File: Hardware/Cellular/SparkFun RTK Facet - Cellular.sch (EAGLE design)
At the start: 64 parts, among them IC1 SN74AVC4T774PW, J1 FPC_12_0.5MM_BACKFLIP, J18 SARA_USB, J2 NANO_SIM, J3 U.FL, J6 DIAG, Q2 310mA/60V/1.6Ω, Q3 310mA/60V/1.6Ω, Q4 310mA/60V/1.6Ω, Q5 20V/0.2A/8MHz/1.2Ω/1Vth, Q7 310mA/60V/1.6Ω, U1 SARA-R510M8S, U8 74HC1G04

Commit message: Paul edits. Move dummy to sub-folder
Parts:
- removed C19: 27pF, New_Parts:27PF-0402-25V-5%-X7R
- removed C22: 0.1uF, SparkFun-Capacitors:0.1UF-0603-25V-(+80/-20%)
- removed C24: 15pF, SparkFun-Capacitors:15PF-0603-50V-5%
- removed D10: PESD0402, New_Parts:PESD0402
- removed D13: BLUE, SparkFun-LED:LED-BLUE0603
- removed D14: WHITE, SparkFun-LED:LED-WHITE0603
- removed D8: DT1042-04SO-7, ublox:TVS_DIODE_ARRAY_4DT1042-04SO-7
- removed FRAME1: FRAME-LETTER, SparkFun-Aesthetics:FRAME-LETTER
- removed FRAME2: FRAME-LETTERNO_PACKAGE, SparkFun-Aesthetics:FRAME-LETTERNO_PACKAGE
- removed J18: SARA_USB, SparkFun-Connectors:CONN_041X04_NO_SILK
- removed J6: DIAG, SparkFun-Connectors:CONN_05NO_SILK
- removed JP19: JUMPER-SMT_3_1-NC_TRACE_SILK, SparkFun-Jumpers:JUMPER-SMT_3_1-NC_TRACE_SILK
- removed L2: 68nH, New_Parts:68NH-0402
- removed Q4, Q7: 310mA/60V/1.6Ω, SparkFun-DiscreteSemi:MOSFET-NCH-2N7002PW
- removed Q5: 20V/0.2A/8MHz/1.2Ω/1Vth, SparkFun-DiscreteSemi:MOSFET-NCH-RE1C00UNTL
- removed R18, R19, R39, R44: 100k, SparkFun-Resistors:100KOHM-0603-1/10W-1%
- removed R23: 10k, SparkFun-Resistors:10KOHM-0603-1/10W-1%
- removed R27, R28, R34, R42, R43: 1k, SparkFun-Resistors:1KOHM-0603-1/10W-1%
- removed R29, R30: 2.2k, SparkFun-Resistors:2.2KOHM-0603-1/10W-1%
- removed R31: 0, SparkFun-Resistors:0OHM-0603-1/10W
- removed R35: 470, SparkFun-Resistors:470OHM-0603-1/10W-1%
- removed TP13: TEST-POINT3, SparkFun-Connectors:TEST-POINT3
- removed U8: 74HC1G04, SparkFun-IC-Logic:74HC1G04
- added C1, C17, C3: 1.0uF, SparkFun-Capacitors:1.0UF-0603-16V-10%-X7R
- added C13: 33pF, New_Parts:33PF-0402-25V-5%-X7R
- added C2, C4, C5, C6: 0.1uF, SparkFun-Capacitors:0.1UF-0603-25V-5%
- added C9: 47pF, SparkFun-Capacitors:47PF-0603-50V-5%
- added D1: PESD0402, New_Parts:PESD0402
- added D2: DT1042-04SO-7, ublox:TVS_DIODE_ARRAY_4DT1042-04SO-7
- added FRAME3: FRAME-LEDGER, SparkFun-Aesthetics:FRAME-LEDGER
- added J4: (no value), SparkFun-Connectors:SIMHOLDER-PUSHPUSH
- added LOGO1: SPECIAL_INSTRUCTIONS-ORDERING, SparkFun-Aesthetics:SPECIAL_INSTRUCTIONS-ORDERING
- added Q1: 20V/0.2A/8MHz/1.2Ω/1Vth, SparkFun-DiscreteSemi:MOSFET-NCH-RE1C002UNTCL
- added R1, R2, R3: 100k, SparkFun-Resistors:100KOHM-0603-1/10W-1%
- added R4, R5: 1k, SparkFun-Resistors:1KOHM-0603-1/10W-1%
- added R6, R7: 2.2k, SparkFun-Resistors:2.2KOHM-0603-1/10W-1%
- added R8: 0, SparkFun-Resistors:0OHM-0603-1/10W
- added TP10, TP11, TP9: TEST-POINT3, SparkFun-Connectors:TEST-POINT3
- added U2: 74HC1G04, SparkFun-IC-Logic:74HC1G04
- added U3: AP2112K-3.3, SparkFun-IC-Power:V_REG_AP2112K-3.3V
- C11: value 47pF -> 68pF; device SparkFun-Capacitors:47PF-0603-50V-5% -> SparkFun-Capacitors:68PF-0603-50V-5%
- C12: value 0.1uF -> 10uF; device SparkFun-Capacitors:0.1UF-0603-25V-5% -> SparkFun-Capacitors:10UF-0603-6.3V-20%
- C14: device SparkFun-Capacitors:0.1UF-0603-25V-5% -> SparkFun-Capacitors:0.1UF-0603-25V-(+80/-20%)
- C15: value 68pF -> 15pF; device SparkFun-Capacitors:68PF-0603-50V-5% -> SparkFun-Capacitors:15PF-0603-50V-5%
- C16: value 10uF -> 0.1uF; device SparkFun-Capacitors:10UF-0603-6.3V-20% -> SparkFun-Capacitors:0.1UF-0603-25V-(+80/-20%)
- C18: value 33pF -> 0.1uF; device New_Parts:33PF-0402-25V-5%-X7R -> SparkFun-Capacitors:0.1UF-0603-25V-5%
- J2: value NANO_SIM -> U.FL; device ublox:NANO_SIMWURTH -> SparkFun-Connectors:U.FL2PIN
- J3: value U.FL -> DIAG; device SparkFun-Connectors:U.FL2PIN -> SparkFun-Connectors:CONN_06NO_SILK_FEMALE_PTH
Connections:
- removed net 1.8V: J6.4
- removed net LTE_NI: Q3.D, R35.1, R39.1
- removed net N$16: C19.1, D10.1, L2.1, R23.2
- removed net N$35: Q3.G, R34.2
- removed net N$37: D13.C, R35.2
- removed net N$43: JP19.2, Q5.S, R29.1
- removed net N$47: Q7.G, R42.2
- removed net N$49: D14.C, R43.2
- removed net SARA_!ON!: Q7.D, R43.1, R44.1, TP13.1
- removed net SARA_ANT_DET: R23.1, U1.ANT_DET
- removed net SARA_GPIO3: JP19.1
- removed net SARA_NI: R34.1, U1.GPIO1
- removed net SARA_TP: U1.GPIO6/TP
- removed net SARA_USB_D+: J18.2, U1.USB_D+
- removed net SARA_USB_D-: J18.1, U1.USB_D-
- removed net SARA_VUSB_DET: J18.3, U1.VUSB_DET
- removed net VIN: J6.1
- new net MAIN_3V3: J1.10, J1.9, R1.2, U3.EN
- new net N$1: TP9.1, U1.USB_D-
- new net N$2: TP10.1, U1.USB_D+
- new net N$3: TP11.1, U1.VUSB_DET
- net 3.3V: now also C11.1, C12.1, C3.1, C4.2, C6.1, J3.2, R7.2, U2G2.P$V+, U3.OUT; no longer C14.1, C24.1, D13.A, D14.A, J1.3, J1.4, J6.2, R30.2, R39.2, R44.2, U8G2.P$V+
- net GND: now also C1.2, C11.2, C12.2, C17.2, C18.1, C2.1, C3.2, C4.1, C5.1, C6.2, C9.1, D1.2, D2.2, D2.5, J1.11, J1.12, J3.6, J4.GND, R1.1, R2.2, R3.1, U1.DTR_I, U2G2.P$V-, U3.GND; no longer C11.1, C12.1, C19.2, C22.2, C24.2, D10.2, D8.2, D8.5, J1.1, J1.2, J18.4, J3.GND, J6.5, Q4.S, Q7.S, R18.2, R19.1, U8G2.P$V-
- net LTE_!RESET!: now also J1.8, U2G1.A; no longer J1.5, U8G1.A
- net LTE_CTSI: now also J1.5, R3.2; no longer J1.8, R19.2
- net LTE_INT: now also J1.6, Q1.D, R7.1; no longer J1.7, Q5.D, R30.1
- net LTE_PWR_ON: now also J1.7, R2.1, R4.1; no longer J1.6, R18.1, R27.1
- net LTE_RTSO: now also J1.4; no longer J1.9
- net LTE_RXI: now also J1.3, J3.4; no longer J1.10
- net LTE_TXO: now also J1.2, J3.5; no longer J1.11
- net N$15: now also C13.2, D1.1, J2.SIGNAL; no longer C18.2, J3.SIGNAL, L2.2
- net N$26: now also R4.2; no longer R27.2
- net N$27: now also Q3.G, R5.2; no longer Q4.G, R28.2
- net N$28: now also R5.1, U2G1.Y; no longer R28.1, U8G1.Y
- net N$31: now also C17.1, C18.2, R8.2; no longer R31.2
- net SARA_!RESET!: now also Q3.D; no longer Q4.D
- net SARA_ANT: now also C13.1; no longer C18.1
- net SARA_EXT_INT: now also Q1.S, R6.1; no longer JP19.3
- net SIM_CLK: now also D2.4, J4.CLK; no longer D8.1, J2.CLK
- net SIM_IO: now also D2.6, J4.I/O; no longer D8.6, J2.IO
- net SIM_RST: now also D2.3, J4.RST; no longer D8.4, J2.RST
- net VCCIO: now also C14.1, J3.3, Q1.G, R6.2, R8.1; no longer C22.1, J6.3, Q5.G, R29.2, R31.1, R42.1
- net VOUT: now also C1.1, C2.2, J1.1, J3.1, U3.IN; no longer J1.12
- net VSIM: now also C5.2, C9.2, D2.1, J4.VCC; no longer C11.2, C12.2, D8.3, J2.VCC
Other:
- note added: "600mA Max 55uA Quiescent"
- note added: "JLCPCB JLC7628 4-layer Impedance Control"
- note added: "Paul Clark"
- note added: "VCC: Min. 3.3V Typ. 3.8V Max. 4.4V VCC Extended: Min. 3.0V Max. 4.5V Worst case: Maximum current draw during Tx: 395mA AP2112-3.3 drop out voltage: ~175mV at: 400mA output current; Vout = 3.3V; 25°C Typical: Typical current draw during Tx/Rx: 195mA at 23dBm AP2112-3.3 drop out voltage: ~125mV at: 300mA output current; Vout = 3.3V; 25°C"
- note added: "Voltage Regulation"
- note removed: "SARA LEDs"
- note removed: "VCC: Min. 3.3V Typ. 3.8V Max. 4.4V VCC Extended: Min. 3.0V Max. 4.5V Worst case: Maximum current draw during Tx: 395mA Estimated current for other components: 100mA Total maximum current draw: ~500mA AP7361C-33 drop out voltage: ~170mV at: 500mA output current; Vout = 3.3V; 25°C D7 LSM115J Schottky diode forward voltage: ~210mV at: 500mA; 25°C AP7361C 3.3V output will start to fall when the batte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"

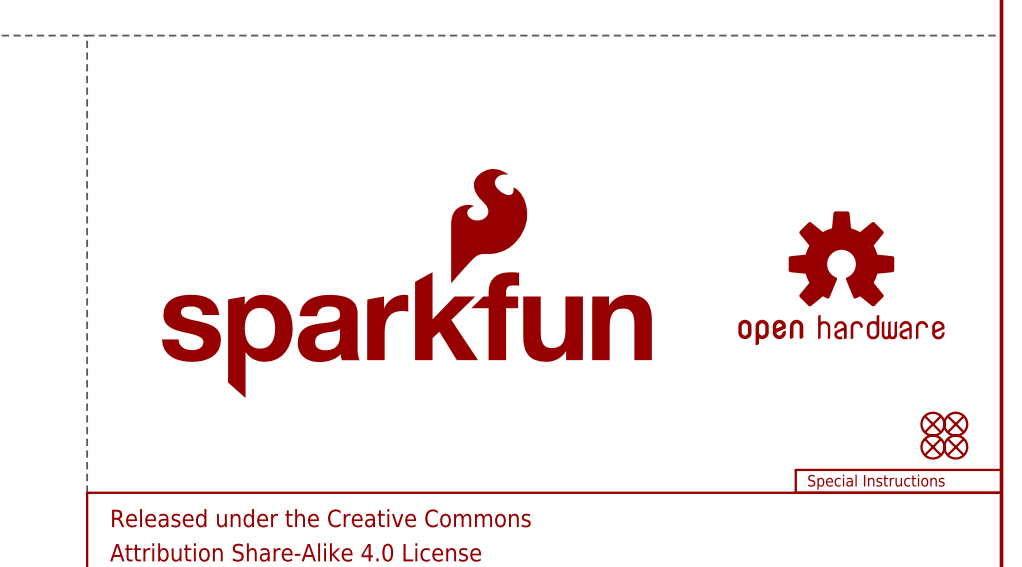
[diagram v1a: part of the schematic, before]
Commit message: Add Buzzard text
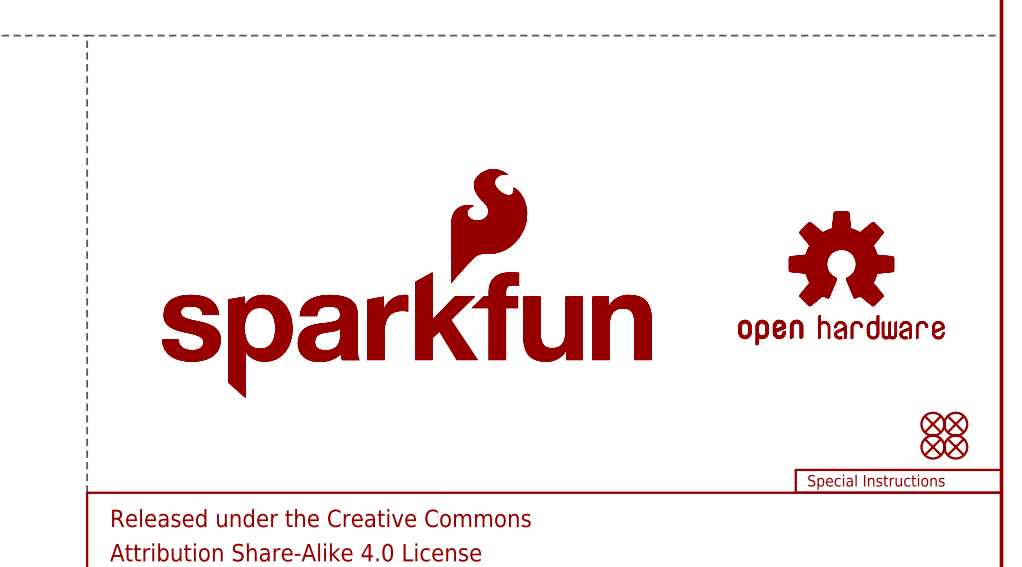
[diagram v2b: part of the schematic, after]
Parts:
- added LOGO2: SFE_LOGO_NAME_FLAME.1_INCH, SparkFun-Aesthetics:SFE_LOGO_NAME_FLAME.1_INCH
- added LOGO4: OSHW-LOGOMINI, SparkFun-Aesthetics:OSHW-LOGOMINI
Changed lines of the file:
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@@
 <part name="GND8" library="SparkFun-PowerSymbols" deviceset="GND" device=""/>
 <part name="GND9" library="SparkFun-PowerSymbols" deviceset="GND" device=""/>
+<part name="LOGO2" library="SparkFun-Aesthetics" deviceset="SFE_LOGO_NAME_FLAME" device=".1_INCH"/>
+<part name="LOGO4" library="SparkFun-Aesthetics" deviceset="OSHW-LOGO" device="MINI" value="OSHW-LOGOMINI"/>
 </parts>
 <sheets>
@@
 <attribute name="VALUE" x="55.88" y="220.726" size="1.778" layer="96" align="top-center"/>
 </instance>
+<instance part="LOGO2" gate="G$1" x="337.82" y="45.72" smashed="yes"/>
+<instance part="LOGO4" gate="G$1" x="414.02" y="60.96" smashed="yes"/>
 </instances>
 <busses>

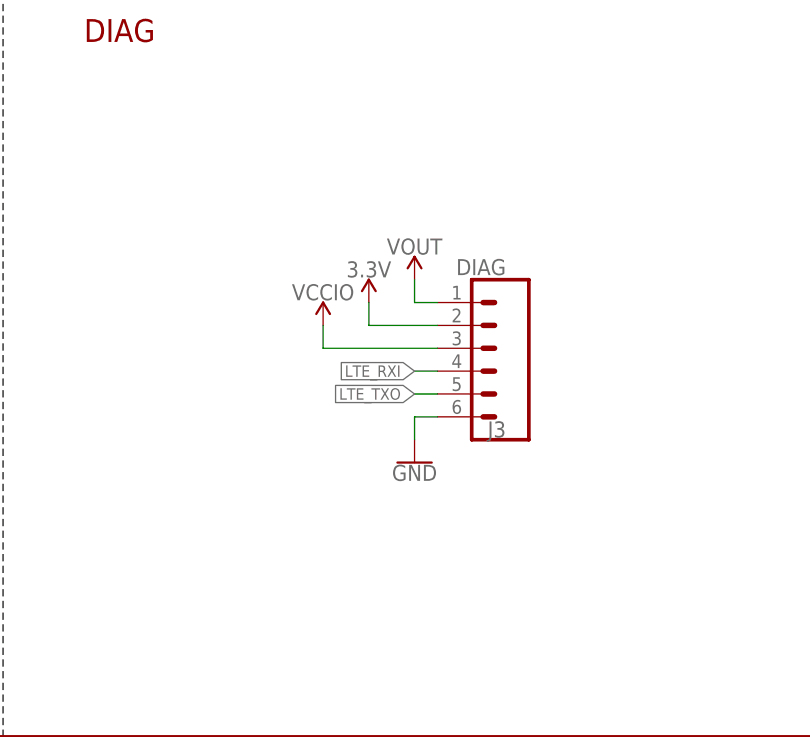
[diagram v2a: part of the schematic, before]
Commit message: Add cellular board production files
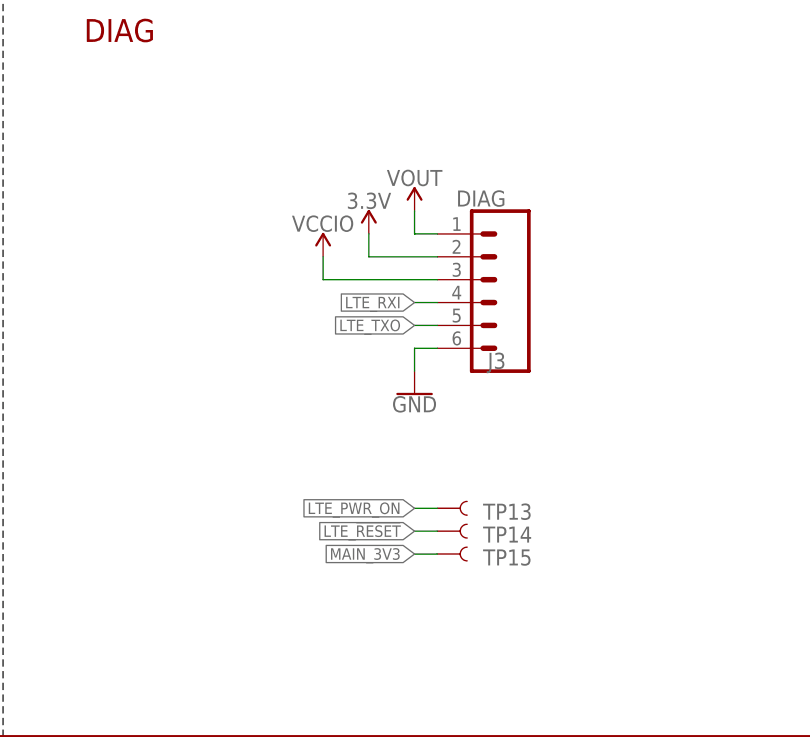
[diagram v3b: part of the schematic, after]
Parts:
- added TP13, TP14, TP15: TEST-POINT3, SparkFun-Connectors:TEST-POINT3
- J4: device SparkFun-Connectors:SIMHOLDER-PUSHPUSH -> SparkFun-Connectors:SIMHOLDER-PUSHPUSH-REDUCED-PADS
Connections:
- net LTE_!RESET!: now also TP14.1
- net LTE_PWR_ON: now also TP13.1
- net MAIN_3V3: now also TP15.1
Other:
- moved on the sheet: J3
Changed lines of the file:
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@@
 <setting verticaltext="up"/>
 </settings>
-<grid distance="0.1" unitdist="inch" unit="inch" style="lines" multiple="1" display="no" altdistance="0.05" altunitdist="inch" altunit="inch"/>
+<grid distance="0.05" unitdist="inch" unit="inch" style="lines" multiple="1" display="yes" altdistance="0.005" altunitdist="inch" altunit="inch"/>
 <layers>
 <layer number="1" name="Top" color="4" fill="1" visible="no" active="no"/>
@@
 <layer number="154" name="FabDoc2" color="7" fill="1" visible="yes" active="yes"/>
 <layer number="155" name="FabDoc3" color="7" fill="1" visible="yes" active="yes"/>
+<layer number="156" name="gesam-Maß" color="1" fill="7" visible="no" active="no"/>
+<layer number="157" name="FaceMchng" color="3" fill="1" visible="no" active="no"/>
+<layer number="158" name="FaceMMeas" color="3" fill="1" visible="no" active="no"/>
+<layer number="159" name="Geh-Bear2" color="1" fill="7" visible="no" active="no"/>
+<layer number="160" name="Topologie" color="9" fill="1" visible="no" active="no"/>
+<layer number="161" name="tomplace2" color="7" fill="1" visible="no" active="no"/>
 <layer number="166" name="AntennaArea" color="7" fill="1" visible="no" active="no"/>
 <layer number="168" name="4mmHeightArea" color="7" fill="1" visible="no" active="no"/>
@@
 <layer number="250" name="Descript" color="7" fill="1" visible="yes" active="yes"/>
 <layer number="251" name="SMDround" color="7" fill="1" visible="yes" active="yes"/>
+<layer number="252" name="BR-BS" color="7" fill="1" visible="no" active="no"/>
 <layer number="253" name="Extra" color="7" fill="1" visible="no" active="no"/>
 <layer number="254" name="cooling" color="7" fill="1" visible="yes" active="yes"/>
@@
 <part name="J2" library="SparkFun-Connectors" deviceset="U.FL2PIN" device="" value="U.FL"/>
 <part name="SUPPLY1" library="SparkFun-PowerSymbols" deviceset="VOUT" device=""/>
-<part name="J4" library="SparkFun-Connectors" deviceset="SIMHOLDER" device="-PUSHPUSH"/>
+<part name="J4" library="SparkFun-Connectors" deviceset="SIMHOLDER" device="-PUSHPUSH-REDUCED-PADS"/>
 <part name="FRAME3" library="SparkFun-Aesthetics" deviceset="FRAME-LEDGER" device=""/>
 <part name="LOGO1" library="SparkFun-Aesthetics" deviceset="SPECIAL_INSTRUCTIONS" device="-ORDERING"/>
@@
 <part name="LOGO2" library="SparkFun-Aesthetics" deviceset="SFE_LOGO_NAME_FLAME" device=".1_INCH"/>
 <part name="LOGO4" library="SparkFun-Aesthetics" deviceset="OSHW-LOGO" device="MINI" value="OSHW-LOGOMINI"/>
+<part name="TP13" library="SparkFun-Connectors" deviceset="TEST-POINT" device="3" value="TEST-POINT3"/>
+<part name="TP14" library="SparkFun-Connectors" deviceset="TEST-POINT" device="3" value="TEST-POINT3"/>
+<part name="TP15" library="SparkFun-Connectors" deviceset="TEST-POINT" device="3" value="TEST-POINT3"/>
 </parts>
 <sheets>
@@
 <attribute name="VALUE" x="332.74" y="134.366" size="1.778" layer="96" align="top-center"/>
 </instance>
-<instance part="J3" gate="G$1" x="287.02" y="43.18" smashed="yes" rot="R180">
-<attribute name="VALUE" x="289.56" y="53.086" size="1.778" layer="96" font="vector" rot="R180"/>
-<attribute name="NAME" x="289.56" y="35.052" size="1.778" layer="95" font="vector" rot="R180"/>
-</instance>
-<instance part="GND17" gate="1" x="279.4" y="30.48" smashed="yes">
-<attribute name="VALUE" x="279.4" y="30.226" size="1.778" layer="96" align="top-center"/>
-</instance>
-<instance part="SUPPLY45" gate="G$1" x="274.32" y="48.26" smashed="yes">
-<attribute name="VALUE" x="274.32" y="51.054" size="1.778" layer="96" align="bottom-center"/>
-</instance>
-<instance part="SUPPLY47" gate="G$1" x="269.24" y="45.72" smashed="yes">
-<attribute name="VALUE" x="269.24" y="48.514" size="1.778" layer="96" align="bottom-center"/>
+<instance part="J3" gate="G$1" x="287.02" y="50.8" smashed="yes" rot="R180">
+<attribute name="VALUE" x="289.56" y="60.706" size="1.778" layer="96" font="vector" rot="R180"/>
+<attribute name="NAME" x="289.56" y="42.672" size="1.778" layer="95" font="vector" rot="R180"/>
+</instance>
+<instance part="GND17" gate="1" x="279.4" y="38.1" smashed="yes">
+<attribute name="VALUE" x="279.4" y="37.846" size="1.778" layer="96" align="top-center"/>
+</instance>
+<instance part="SUPPLY45" gate="G$1" x="274.32" y="55.88" smashed="yes">
+<attribute name="VALUE" x="274.32" y="58.674" size="1.778" layer="96" align="bottom-center"/>
+</instance>
+<instance part="SUPPLY47" gate="G$1" x="269.24" y="53.34" smashed="yes">
+<attribute name="VALUE" x="269.24" y="56.134" size="1.778" layer="96" align="bottom-center"/>
 </instance>
 <instance part="GND32" gate="1" x="99.06" y="104.14" smashed="yes">
@@
 <attribute name="VALUE" x="185.42" y="124.714" size="1.778" layer="96" align="bottom-center"/>
 </instance>
-<instance part="SUPPLY3" gate="G$1" x="279.4" y="50.8" smashed="yes">
-<attribute name="VALUE" x="279.4" y="53.594" size="1.778" layer="96" align="bottom-center"/>
+<instance part="SUPPLY3" gate="G$1" x="279.4" y="58.42" smashed="yes">
+<attribute name="VALUE" x="279.4" y="61.214" size="1.778" layer="96" align="bottom-center"/>
 </instance>
 <instance part="GND6" gate="1" x="63.5" y="218.44" smashed="yes">
@@
 <instance part="LOGO2" gate="G$1" x="337.82" y="45.72" smashed="yes"/>
 <instance part="LOGO4" gate="G$1" x="414.02" y="60.96" smashed="yes"/>
+<instance part="TP13" gate="G$1" x="281.94" y="25.4" smashed="yes">
+<attribute name="NAME" x="287.02" y="24.13" size="1.778" layer="95" font="vector"/>
+</instance>
+<instance part="TP14" gate="G$1" x="281.94" y="22.86" smashed="yes">
+<attribute name="NAME" x="287.02" y="21.59" size="1.778" layer="95" font="vector"/>
+</instance>
+<instance part="TP15" gate="G$1" x="281.94" y="20.32" smashed="yes">
+<attribute name="NAME" x="287.02" y="19.05" size="1.778" layer="95" font="vector"/>
+</instance>
 </instances>
 <busses>
@@
 <segment>
 <pinref part="J3" gate="G$1" pin="6"/>
-<wire x1="281.94" y1="35.56" x2="279.4" y2="35.56" width="0.1524" layer="91"/>
+<wire x1="281.94" y1="43.18" x2="279.4" y2="43.18" width="0.1524" layer="91"/>
 <pinref part="GND17" gate="1" pin="GND"/>
-<wire x1="279.4" y1="35.56" x2="279.4" y2="33.02" width="0.1524" layer="91"/>
+<wire x1="279.4" y1="43.18" x2="279.4" y2="40.64" width="0.1524" layer="91"/>
 </segment>
 <segment>
@@
 <segment>
 <pinref part="J3" gate="G$1" pin="2"/>
-<wire x1="281.94" y1="45.72" x2="274.32" y2="45.72" width="0.1524" layer="91"/>
+<wire x1="281.94" y1="53.34" x2="274.32" y2="53.34" width="0.1524" layer="91"/>
 <pinref part="SUPPLY45" gate="G$1" pin="3.3V"/>
-<wire x1="274.32" y1="45.72" x2="274.32" y2="48.26" width="0.1524" layer="91"/>
+<wire x1="274.32" y1="53.34" x2="274.32" y2="55.88" width="0.1524" layer="91"/>
 </segment>
 <segment>
@@
 <label x="322.58" y="220.98" size="1.27" layer="95" rot="R180" xref="yes"/>
 </segment>
+<segment>
+<pinref part="TP14" gate="G$1" pin="1"/>
+<wire x1="281.94" y1="22.86" x2="279.4" y2="22.86" width="0.1524" layer="91"/>
+<label x="279.4" y="22.86" size="1.27" layer="95" font="vector" rot="R180" xref="yes"/>
+</segment>
 </net>
 <net name="LTE_INT" class="0">
@@
 <junction x="340.36" y="248.92"/>
 </segment>
+<segment>
+<pinref part="TP13" gate="G$1" pin="1"/>
+<wire x1="281.94" y1="25.4" x2="279.4" y2="25.4" width="0.1524" layer="91"/>
+<label x="279.4" y="25.4" size="1.27" layer="95" font="vector" rot="R180" xref="yes"/>
+</segment>
 </net>
 <net name="LTE_TXO" class="0">
@@
 </segment>
 <segment>
-<label x="279.4" y="38.1" size="1.27" layer="95" rot="R180" xref="yes"/>
-<wire x1="281.94" y1="38.1" x2="279.4" y2="38.1" width="0.1524" layer="91"/>
+<label x="279.4" y="45.72" size="1.27" layer="95" rot="R180" xref="yes"/>
+<wire x1="281.94" y1="45.72" x2="279.4" y2="45.72" width="0.1524" layer="91"/>
 <pinref part="J3" gate="G$1" pin="5"/>
 </segment>
@@
 </segment>
 <segment>
-<label x="279.4" y="40.64" size="1.27" layer="95" rot="R180" xref="yes"/>
-<wire x1="281.94" y1="40.64" x2="279.4" y2="40.64" width="0.1524" layer="91"/>
+<label x="279.4" y="48.26" size="1.27" layer="95" rot="R180" xref="yes"/>
+<wire x1="281.94" y1="48.26" x2="279.4" y2="48.26" width="0.1524" layer="91"/>
 <pinref part="J3" gate="G$1" pin="4"/>
 </segment>
@@
 <segment>
 <pinref part="J3" gate="G$1" pin="3"/>
-<wire x1="281.94" y1="43.18" x2="269.24" y2="43.18" width="0.1524" layer="91"/>
+<wire x1="281.94" y1="50.8" x2="269.24" y2="50.8" width="0.1524" layer="91"/>
 <pinref part="SUPPLY47" gate="G$1" pin="VCCIO"/>
-<wire x1="269.24" y1="43.18" x2="269.24" y2="45.72" width="0.1524" layer="91"/>
+<wire x1="269.24" y1="50.8" x2="269.24" y2="53.34" width="0.1524" layer="91"/>
 </segment>
 <segment>
@@
 <segment>
 <pinref part="J3" gate="G$1" pin="1"/>
-<wire x1="281.94" y1="48.26" x2="279.4" y2="48.26" width="0.1524" layer="91"/>
+<wire x1="281.94" y1="55.88" x2="279.4" y2="55.88" width="0.1524" layer="91"/>
 <pinref part="SUPPLY3" gate="G$1" pin="VOUT"/>
-<wire x1="279.4" y1="48.26" x2="279.4" y2="50.8" width="0.1524" layer="91"/>
+<wire x1="279.4" y1="55.88" x2="279.4" y2="58.42" width="0.1524" layer="91"/>
 </segment>
 </net>
@@
 <label x="215.9" y="116.84" size="1.27" layer="95" rot="R180" xref="yes"/>
 </segment>
-</net>
+<segment>
+<pinref part="TP15" gate="G$1" pin="1"/>
+<wire x1="281.94" y1="20.32" x2="279.4" y2="20.32" width="0.1524" layer="91"/>
+<label x="279.4" y="20.32" size="1.27" layer="95" font="vector" rot="R180" xref="yes"/>
+</segment>
+</net>
